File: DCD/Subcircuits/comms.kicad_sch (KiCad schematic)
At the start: 0 parts

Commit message: Finished the schematics. Fixed the comments that we recieved
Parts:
- added J1, J2, J3, J4: UMPS-04-03.5-G-VT-SM-WT, LOBSTER:UMPS-04-03.5-G-VT-SM-WT, symbol Connector:Conn_01x04_Female
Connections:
- new net *CS1: J3.2 (Pin_2)
- new net *CS2: J3.4 (Pin_4)
- new net BSY: J2.3 (Pin_3)
- new net CLK: J2.4 (Pin_4)
- new net CNV: J2.2 (Pin_2)
- new net Ext: J4.4 (Pin_4)
- new net GND: J4.3 (Pin_3)
- new net SCK: J1.4 (Pin_4)
- new net SDI: J2.1 (Pin_1)
- new net SDI1: J3.1 (Pin_1)
- new net SDI2: J3.3 (Pin_3)
- new net SDO0: J1.1 (Pin_1)
- new net SDO1: J1.2 (Pin_2)
- new net VRef: J4.2 (Pin_2)
- new net Vin: J4.1 (Pin_1)
- new net ~{CS}: J1.3 (Pin_3)

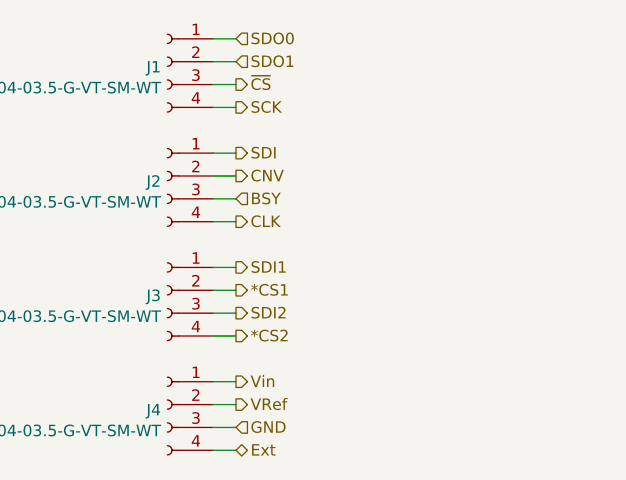
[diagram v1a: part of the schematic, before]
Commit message: Finished
Final touches, PSUs filtering, external connections, psu connections for
the negative voltage, and the DAC higher voltage, and the negative
voltage. Added an external connection directely to the DAC.
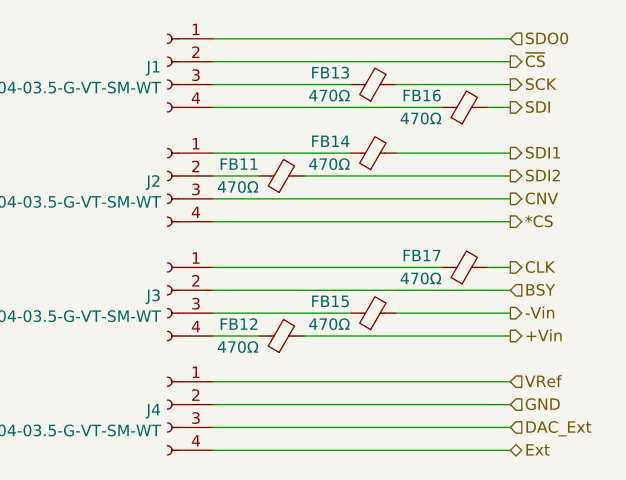
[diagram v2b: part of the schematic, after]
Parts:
- added FB11, FB12, FB13, FB14, FB15, FB16, FB17: 470Ω, Inductor_SMD:L_0603_1608Metric, symbol Device:FerriteBead_Small
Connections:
- net *CS1 is gone; now on net BSY: J3.2 (Pin_2)
- net SDO1 is gone; now on net ~{CS}: J1.2 (Pin_2)
- net Vin is gone; now on net VRef: J4.1 (Pin_1)
- net BSY: no longer J2.3 (Pin_3)
- net CLK: now also FB17.2; no longer J2.4 (Pin_4)
- net CNV: now also J2.3 (Pin_3); no longer J2.2 (Pin_2)
- net GND: now also J4.2 (Pin_2); no longer J4.3 (Pin_3)
- net SCK: now also FB13.2; no longer J1.4 (Pin_4)
- net SDI: now also FB16.2; no longer J2.1 (Pin_1)
- net SDI1: now also FB14.2; no longer J3.1 (Pin_1)
- net SDI2: now also FB11.2; no longer J3.3 (Pin_3)
- net VRef: no longer J4.2 (Pin_2)
- net ~{CS}: no longer J1.3 (Pin_3)
- net *CS2: no longer names the net of J3.4 (Pin_4)
- net *CS2: now also FB12.1
- new net: FB13.1, J1.3 (Pin_3)
- new net: FB16.1, J1.4 (Pin_4)
- new net: FB14.1, J2.1 (Pin_1)
- new net: FB11.1, J2.2 (Pin_2)
- new net: FB17.1, J3.1 (Pin_1)
- new net: FB15.1, J3.3 (Pin_3)
- new net *CS: J2.4 (Pin_4)
- new net +Vin: FB12.2
- new net -Vin: FB15.2
- new net DAC_Ext: J4.3 (Pin_3)

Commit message: Progress on fixing the remaining footprints and 3 models
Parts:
- J1, J2, J3, J4: footprint LOBSTER:UMPS-04-03.5-G-VT-SM-WT -> custom_components:UMPS-04-03.5-G-VT-SM-WT
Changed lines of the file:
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@@
 			)
 		)
-		(property "Footprint" "LOBSTER:UMPS-04-03.5-G-VT-SM-WT"
+		(property "Footprint" "custom_components:UMPS-04-03.5-G-VT-SM-WT"
 			(at 90.17 39.37 0)
 			(effects
@@
 			)
 		)
-		(property "Footprint" "LOBSTER:UMPS-04-03.5-G-VT-SM-WT"
+		(property "Footprint" "custom_components:UMPS-04-03.5-G-VT-SM-WT"
 			(at 90.17 52.07 0)
 			(effects
@@
 			)
 		)
-		(property "Footprint" "LOBSTER:UMPS-04-03.5-G-VT-SM-WT"
+		(property "Footprint" "custom_components:UMPS-04-03.5-G-VT-SM-WT"
 			(at 90.17 64.77 0)
 			(effects
@@
 			)
 		)
-		(property "Footprint" "LOBSTER:UMPS-04-03.5-G-VT-SM-WT"
+		(property "Footprint" "custom_components:UMPS-04-03.5-G-VT-SM-WT"
 			(at 90.17 77.47 0)
 			(effects

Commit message: Progress on the layout
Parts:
- removed FB17: 470Ω, Inductor_SMD:L_0603_1608Metric, symbol Device:FerriteBead_Small
- added J5: Conn_01x02_Pin, Connector_PinHeader_2.54mm:PinHeader_1x02_P2.54mm_Vertical, symbol Connector:Conn_01x02_Pin
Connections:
- net CLK: now also J3.1 (Pin_1)
- net at FB11.1: now also J5.1 (Pin_1); no longer J2.2 (Pin_2)
- net GND renamed AGND
- new net DGND: J2.2 (Pin_2), J5.2 (Pin_2)
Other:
- moved on the sheet: FB13, FB14, FB16

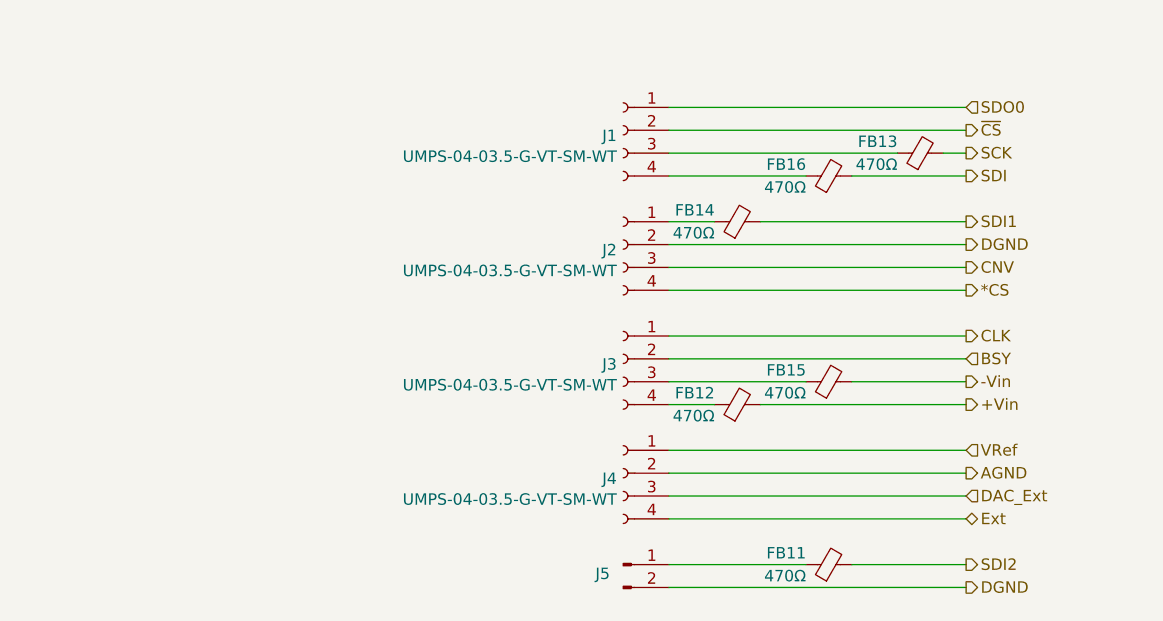
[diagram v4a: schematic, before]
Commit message: Schematics for the clock reconditioning
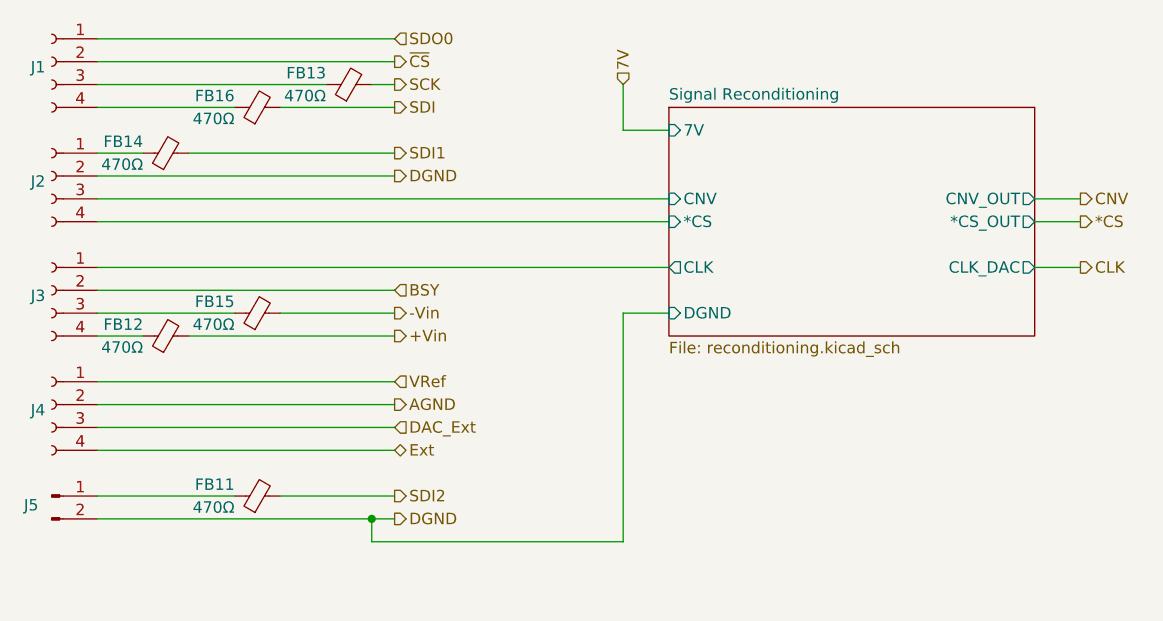
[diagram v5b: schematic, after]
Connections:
- net *CS: no longer J2.4 (Pin_4)
- net CLK: no longer J3.1 (Pin_1)
- net CNV: no longer J2.3 (Pin_3)
- new net Signal Reconditioning/*CS: J2.4 (Pin_4)
- new net Signal Reconditioning/CLK: J3.1 (Pin_1)
- new net Signal Reconditioning/CNV: J2.3 (Pin_3)
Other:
- added sheet Signal Reconditioning (reconditioning.kicad_sch)
- moved on the sheet: FB11, FB12, FB13, FB14, FB15, FB16, J1, J2, J3, J4, J5

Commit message: Layout mostly done
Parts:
- removed J5: Conn_01x02_Pin, Connector_PinHeader_2.54mm:PinHeader_1x02_P2.54mm_Vertical, symbol Connector:Conn_01x02_Pin
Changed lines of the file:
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@@
 	(wire
 		(pts
-			(xy 90.17 85.09) (xy 62.23 85.09)
+			(xy 90.17 77.47) (xy 62.23 77.47)
 		)
 		(stroke
@@
 	(wire
 		(pts
-			(xy 62.23 85.09) (xy 62.23 82.55)
-		)
-		(stroke
-			(width 0)
-			(type default)
-		)
-	)
-	(wire
-		(pts
 			(xy 31.75 57.15) (xy 64.77 57.15)
 		)
@@
 	(wire
 		(pts
-			(xy 90.17 59.69) (xy 90.17 85.09)
+			(xy 62.23 77.47) (xy 62.23 82.55)
+		)
+		(stroke
+			(width 0)
+			(type default)
+		)
+	)
+	(wire
+		(pts
+			(xy 90.17 59.69) (xy 90.17 77.47)
 		)
 		(stroke
@@
 		)
 	)
-	(hierarchical_label "*CS"
+	(hierarchical_label "*CS2"
 		(shape output)
 		(at 140.97 49.53 0)
@@
 		)
 	)
+	(hierarchical_label "CLK2"
+		(shape output)
+		(at 64.77 87.63 0)
+		(effects
+			(font
+				(size 1.27 1.27)
+			)
+			(justify left)
+		)
+	)
 	(hierarchical_label "VRef"
 		(shape input)
@@
 		)
 	)
-	(hierarchical_label "CLK"
+	(hierarchical_label "CLK2"
 		(shape output)
 		(at 140.97 54.61 0)
@@
 		(shape output)
 		(at 64.77 80.01 0)
+		(effects
+			(font
+				(size 1.27 1.27)
+			)
+			(justify left)
+		)
+	)
+	(hierarchical_label "*CS2"
+		(shape output)
+		(at 64.77 85.09 0)
 		(effects
 			(font
@@
 					(unit 1)
 				)
-			)
-		)
-	)
-	(symbol
-		(lib_id "Connector:Conn_01x02_Pin")
-		(at 26.67 80.01 0)
-		(unit 1)
-		(exclude_from_sim no)
-		(in_bom yes)
-		(on_board yes)
-		(dnp no)
-		(property "Reference" "J5"
-			(at 24.384 81.026 0)
-			(effects
-				(font
-					(size 1.27 1.27)
-				)
-			)
-		)
-		(property "Value" "Conn_01x02_Pin"
-			(at 27.305 77.47 0)
-			(effects
-				(font
-					(size 1.27 1.27)
-				)
-				(hide yes)
-			)
-		)
-		(property "Footprint" "Connector_PinHeader_2.54mm:PinHeader_1x02_P2.54mm_Vertical"
-			(at 26.67 80.01 0)
-			(effects
-				(font
-					(size 1.27 1.27)
-				)
-				(hide yes)
-			)
-		)
-		(property "Datasheet" "~"
-			(at 26.67 80.01 0)
-			(effects
-				(font
-					(size 1.27 1.27)
-				)
-				(hide yes)
-			)
-		)
-		(property "Description" "Generic connector, single row, 01x02, script generated"
-			(at 26.67 80.01 0)
-			(effects
-				(font
-					(size 1.27 1.27)
-				)
-				(hide yes)
-			)
-		)
-		(pin "2"
-		)
-		(pin "1"
-		)
-		(instances
-			(project "DCD"
-				(path "/b8e3d55b-fa56-4199-88ad-60cfd98f56f9/650cd0f6-4277-45cc-8777-f2e2a60d96c5"
-					(reference "J5")
-					(unit 1)
-				)

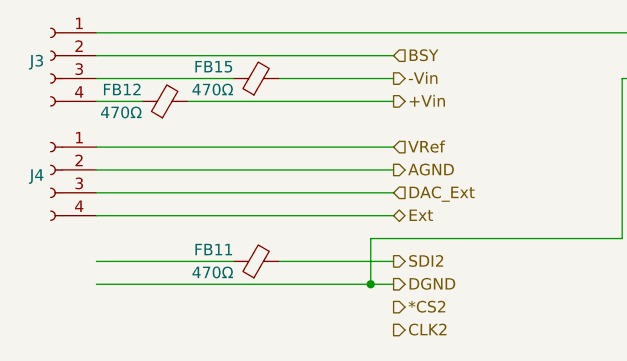
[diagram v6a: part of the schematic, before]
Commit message: Added the pin header
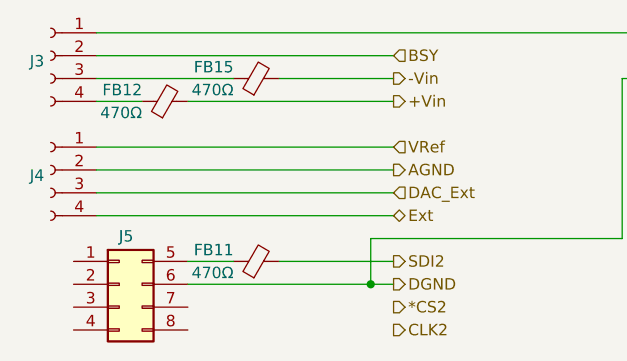
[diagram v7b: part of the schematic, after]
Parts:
- added J5: Conn_02x04_Top_Bottom, Connector_PinHeader_2.54mm:PinHeader_2x04_P2.54mm_Vertical_SMD, symbol Connector_Generic:Conn_02x04_Top_Bottom
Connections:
- net DGND: now also J5.6 (Pin_6)
- net at FB11.1: now also J5.5 (Pin_5)
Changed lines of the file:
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@@
 	(wire
 		(pts
-			(xy 31.75 80.01) (xy 46.99 80.01)
+			(xy 41.91 80.01) (xy 46.99 80.01)
 		)
 		(stroke
@@
 	(wire
 		(pts
-			(xy 31.75 82.55) (xy 62.23 82.55)
+			(xy 41.91 82.55) (xy 62.23 82.55)
 		)
 		(stroke
@@
 					(unit 1)
 				)
+			)
+		)
+	)
+	(symbol
+		(lib_id "Connector_Generic:Conn_02x04_Top_Bottom")
+		(at 34.29 82.55 0)
+		(unit 1)
+		(exclude_from_sim no)
+		(in_bom yes)
+		(on_board yes)
+		(dnp no)
+		(property "Reference" "J5"
+			(at 35.052 77.216 0)
+			(effects
+				(font
+					(size 1.27 1.27)
+				)
+			)
+		)
+		(property "Value" "Conn_02x04_Top_Bottom"
+			(at 35.56 76.2 0)
+			(effects
+				(font
+					(size 1.27 1.27)
+				)
+				(hide yes)
+			)
+		)
+		(property "Footprint" "Connector_PinHeader_2.54mm:PinHeader_2x04_P2.54mm_Vertical_SMD"
+			(at 34.29 82.55 0)
+			(effects
+				(font
+					(size 1.27 1.27)
+				)
+				(hide yes)
+			)
+		)
+		(property "Datasheet" "~"
+			(at 34.29 82.55 0)
+			(effects
+				(font
+					(size 1.27 1.27)
+				)
+				(hide yes)
+			)
+		)
+		(property "Description" "Generic connector, double row, 02x04, top/bottom pin numbering scheme (row 1: 1...pins_per_row, row2: pins_per_row+1 ... num_pins), script generated (kicad-library-utils/schlib/autogen/connector/)"
+			(at 34.29 82.55 0)
+			(effects
+				(font
+					(size 1.27 1.27)
+				)
+				(hide yes)
+			)
+		)
+		(pin "8"
+		)
+		(pin "1"
+		)
+		(pin "2"
+		)
+		(pin "4"
+		)
+		(pin "3"
+		)
+		(pin "7"
+		)
+		(pin "6"
+		)
+		(pin "5"
+		)
+		(instances
+			(project ""
+				(path "/b8e3d55b-fa56-4199-88ad-60cfd98f56f9/650cd0f6-4277-45cc-8777-f2e2a60d96c5"
+					(reference "J5")
+					(unit 1)
+				)

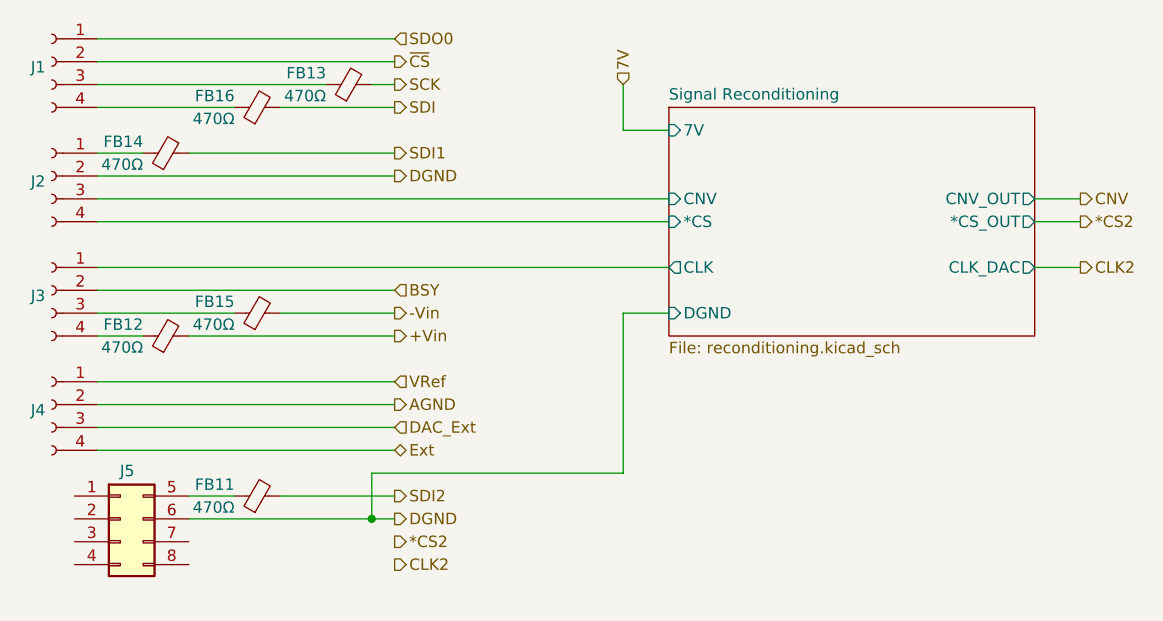
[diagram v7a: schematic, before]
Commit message: Connected the pin header in the schematics
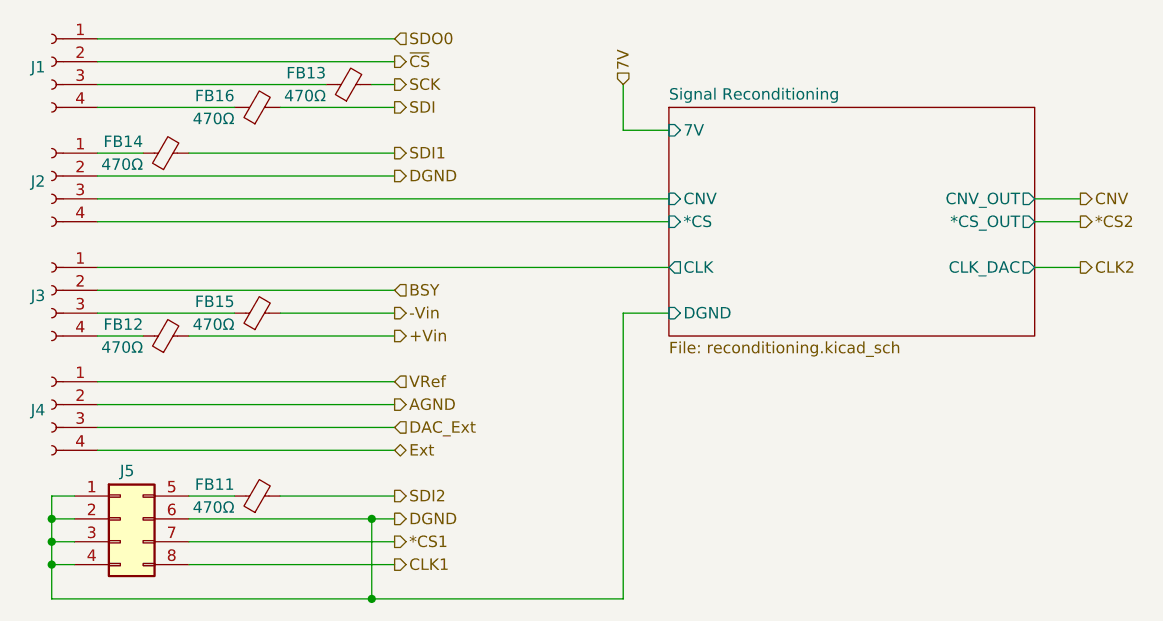
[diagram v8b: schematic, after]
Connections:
- net DGND: now also J5.1 (Pin_1), J5.2 (Pin_2), J5.3 (Pin_3), J5.4 (Pin_4)
- net *CS1: now reaches J5.7 (Pin_7)
- net CLK1: now reaches J5.8 (Pin_8)
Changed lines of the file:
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@@
 	(paper "A5")
+	(junction
+		(at 26.67 87.63)
+		(diameter 0)
+		(color 0 0 0 0)
+	)
+	(junction
+		(at 62.23 91.44)
+		(diameter 0)
+		(color 0 0 0 0)
+	)
+	(junction
+		(at 26.67 85.09)
+		(diameter 0)
+		(color 0 0 0 0)
+	)
+	(junction
+		(at 26.67 82.55)
+		(diameter 0)
+		(color 0 0 0 0)
+	)
 	(junction
 		(at 62.23 82.55)
@@
 	(wire
 		(pts
+			(xy 62.23 91.44) (xy 62.23 82.55)
+		)
+		(stroke
+			(width 0)
+			(type default)
+		)
+	)
+	(wire
+		(pts
 			(xy 31.75 54.61) (xy 95.25 54.61)
 		)
@@
 	(wire
 		(pts
-			(xy 90.17 77.47) (xy 62.23 77.47)
+			(xy 26.67 80.01) (xy 26.67 82.55)
+		)
+		(stroke
+			(width 0)
+			(type default)
+		)
+	)
+	(wire
+		(pts
+			(xy 26.67 91.44) (xy 62.23 91.44)
+		)
+		(stroke
+			(width 0)
+			(type default)
+		)
+	)
+	(wire
+		(pts
+			(xy 41.91 87.63) (xy 64.77 87.63)
+		)
+		(stroke
+			(width 0)
+			(type default)
+		)
+	)
+	(wire
+		(pts
+			(xy 90.17 91.44) (xy 62.23 91.44)
+		)
+		(stroke
+			(width 0)
+			(type default)
+		)
+	)
+	(wire
+		(pts
+			(xy 41.91 85.09) (xy 64.77 85.09)
 		)
 		(stroke
@@
 	(wire
 		(pts
+			(xy 26.67 87.63) (xy 26.67 91.44)
+		)
+		(stroke
+			(width 0)
+			(type default)
+		)
+	)
+	(wire
+		(pts
 			(xy 95.25 59.69) (xy 90.17 59.69)
 		)
@@
 	(wire
 		(pts
+			(xy 26.67 85.09) (xy 26.67 87.63)
+		)
+		(stroke
+			(width 0)
+			(type default)
+		)
+	)
+	(wire
+		(pts
 			(xy 31.75 62.23) (xy 36.83 62.23)
 		)
@@
 	(wire
 		(pts
+			(xy 26.67 85.09) (xy 29.21 85.09)
+		)
+		(stroke
+			(width 0)
+			(type default)
+		)
+	)
+	(wire
+		(pts
+			(xy 26.67 82.55) (xy 26.67 85.09)
+		)
+		(stroke
+			(width 0)
+			(type default)
+		)
+	)
+	(wire
+		(pts
 			(xy 31.75 34.29) (xy 57.15 34.29)
 		)
@@
 	(wire
 		(pts
+			(xy 29.21 80.01) (xy 26.67 80.01)
+		)
+		(stroke
+			(width 0)
+			(type default)
+		)
+	)
+	(wire
+		(pts
 			(xy 135.89 46.99) (xy 140.97 46.99)
 		)
@@
 	(wire
 		(pts
-			(xy 62.23 77.47) (xy 62.23 82.55)
-		)
-		(stroke
-			(width 0)
-			(type default)
-		)
-	)
-	(wire
-		(pts
-			(xy 90.17 59.69) (xy 90.17 77.47)
+			(xy 26.67 82.55) (xy 29.21 82.55)
+		)
+		(stroke
+			(width 0)
+			(type default)
+		)
+	)
+	(wire
+		(pts
+			(xy 26.67 87.63) (xy 29.21 87.63)
+		)
+		(stroke
+			(width 0)
+			(type default)
+		)
+	)
+	(wire
+		(pts
+			(xy 90.17 59.69) (xy 90.17 91.44)
 		)
 		(stroke
@@
 		)
 	)
-	(hierarchical_label "CLK2"
+	(hierarchical_label "CLK1"
 		(shape output)
 		(at 64.77 87.63 0)
@@
 		)
 	)
-	(hierarchical_label "*CS2"
+	(hierarchical_label "*CS1"
 		(shape output)
 		(at 64.77 85.09 0)
@@
 		)
 		(instances
-			(project ""
+			(project "DCD"
 				(path "/b8e3d55b-fa56-4199-88ad-60cfd98f56f9/650cd0f6-4277-45cc-8777-f2e2a60d96c5"
 					(reference "J5")
